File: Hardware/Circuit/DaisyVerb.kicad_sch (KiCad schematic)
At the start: 34 parts, among them J1 AUDIO_IN1, J2 AUDIO_OUT1, J3 AUDIO_IN1, J4 AUDIO_OUT2, U1 TL074, U2 TL074

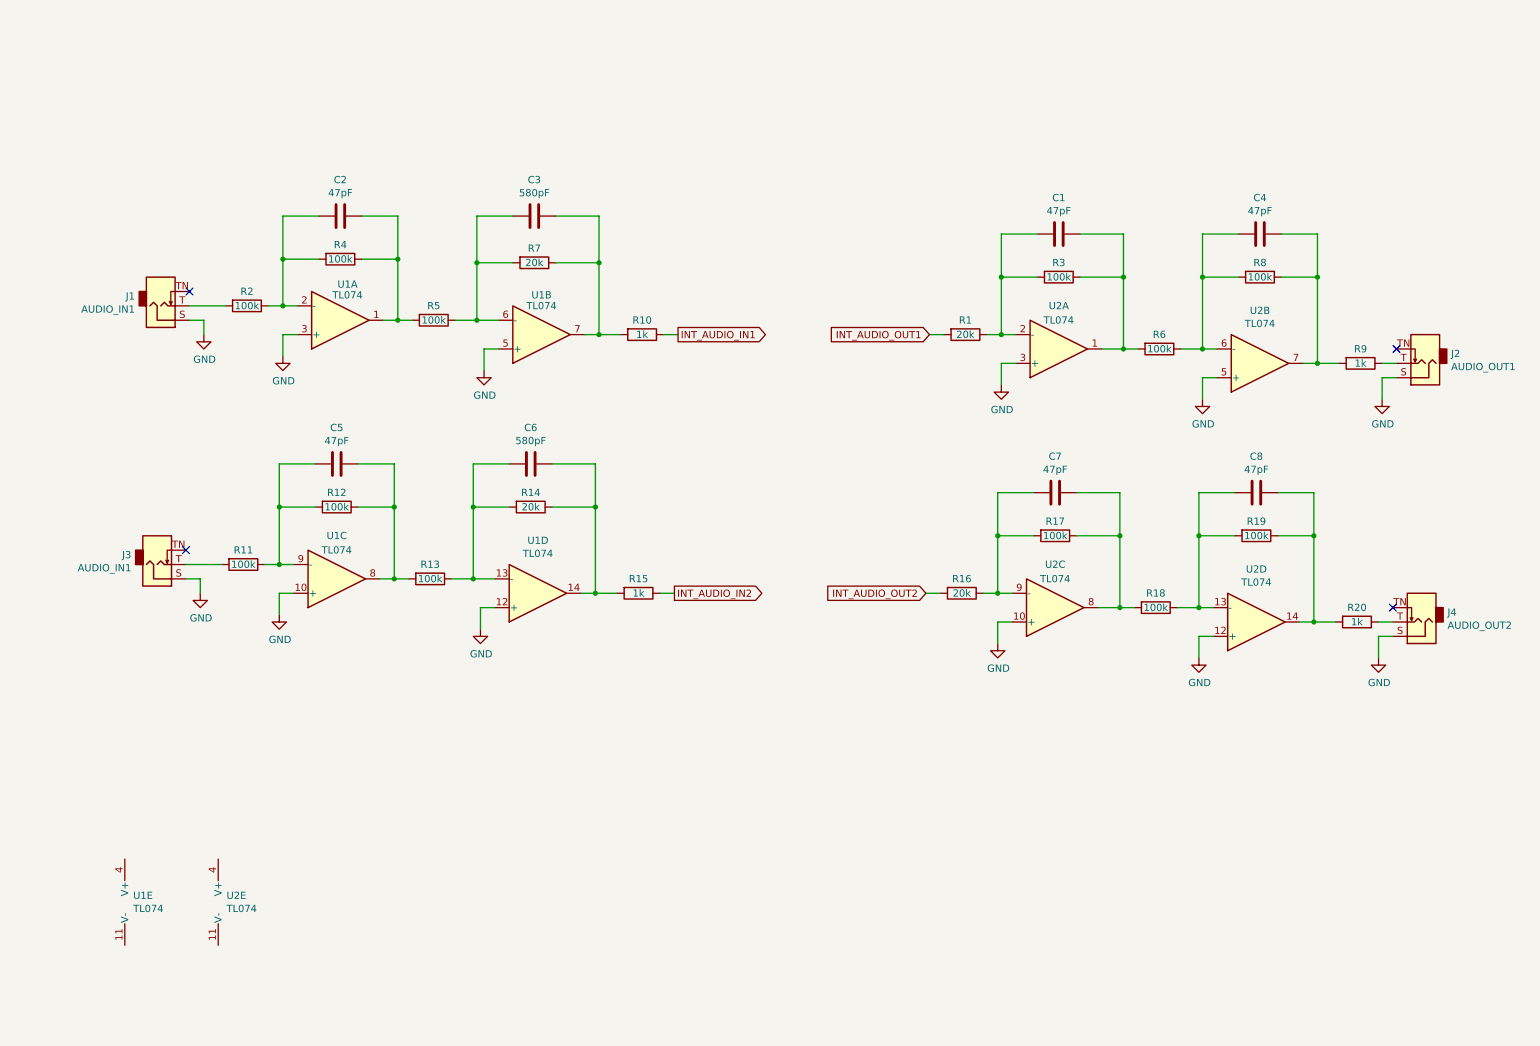
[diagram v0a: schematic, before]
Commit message: Added mode knobs and stuff
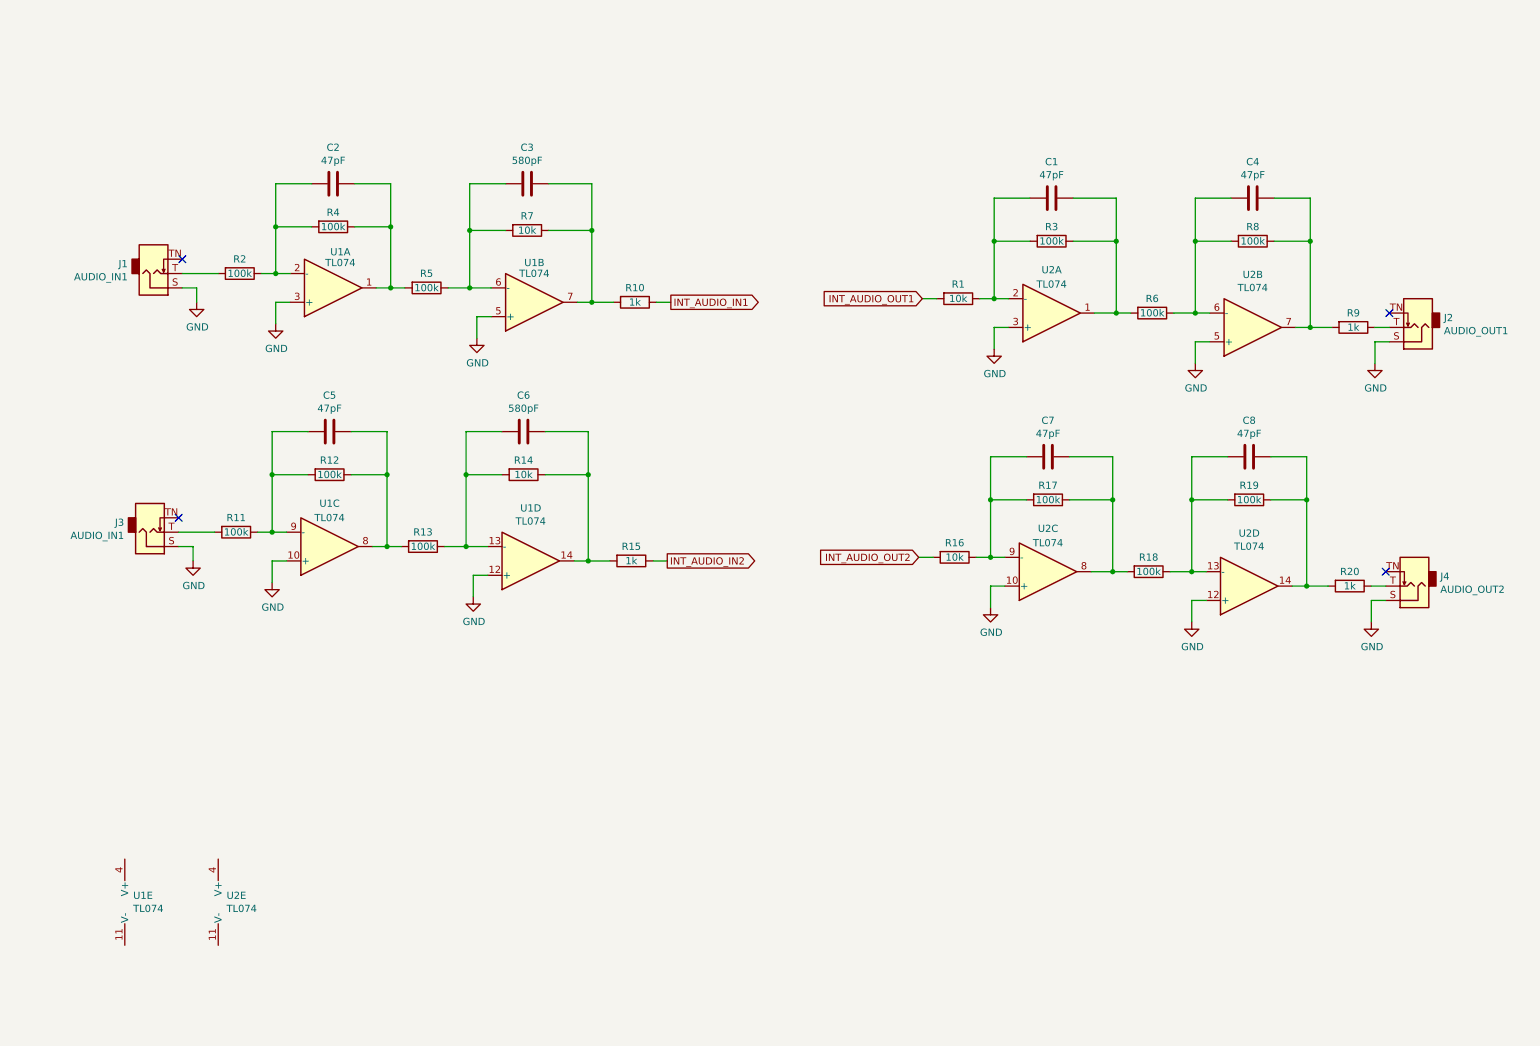
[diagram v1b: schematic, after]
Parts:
- R1, R14, R16, R7: value 20k -> 10k
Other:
- moved on the sheet: C1, C2, C3, C4, C5, C6, C7, C8, J1, J2, J3, J4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

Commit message: Completed schematics
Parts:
- added A?: Device_Audio_Electrosmith_Daisy_Seed_Rev4, daisy-seed:Device_Audio_Electrosmith_Daisy_Seed, symbol Device_Audio_Electrosmith_Daisy_Seed:Device_Audio_Electrosmith_Daisy_Seed_Rev4
- added C? (x2): 100uF, symbol Device:C_Polarized_US
- added POT_DRY, POT_FBK, POT_JTR, POT_LPF, POT_WET: B10K, symbol Device:R_Potentiometer
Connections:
- net GND: now also A?.20 (AGND), A?.40 (GND), C?.1, C?.2, POT_DRY.1, POT_FBK.1, POT_JTR.1, POT_LPF.1, POT_WET.1
- net INT_AUDIO_IN1: now also A?.16 (AUDIO_IN_L)
- net INT_AUDIO_IN2: now also A?.17 (AUDIO_IN_R)
- net INT_AUDIO_OUT1: now also A?.18 (AUDIO_OUT_L)
- net INT_AUDIO_OUT2: now also A?.19 (AUDIO_OUT_R)
- net -12V: now reaches U1.11 (V-)
- net -12V: now also C?.2
- net +12V: now reaches U1.4 (V+)
- net +12V: now also U2.4 (V+), A?.39 (VIN), C?.1
- new net 3V3_A: A?.21 (3V3_A), POT_DRY.3, POT_FBK.3, POT_JTR.3, POT_LPF.3, POT_WET.3
- new net DRY: A?.1 (USB_HS_ID), POT_DRY.2
- new net FEEDBACK: A?.3 (SDMMC1_D2), POT_FBK.2
- new net JITTER: A?.4 (SDMMC1_D1), POT_JTR.2
- new net LPF: A?.5 (SDMMC1_D0), POT_LPF.2
- new net WET: A?.2 (SDMMC1_D3), POT_WET.2
- no-connect marks 4 -> 31
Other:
- note added: "Inputs"
- note added: "Knobs"
- note added: "MCU"
- note added: "Outputs"
- note added: "Power"
- moved on the sheet: C1, C2, C3, C4, C5, C6, C7, C8, J1, J2, J3, J4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
